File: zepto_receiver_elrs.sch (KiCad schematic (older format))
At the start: 43 parts, among them J1 u.fl, SW1 SW_Push, U1 STM32WLE5JBI6, U2 NCP160, U3 BGS12PL6E6327XTSA1, U4 0900FM15D0039, U5 ECS-TXO-25CSMV-320-AM-TR

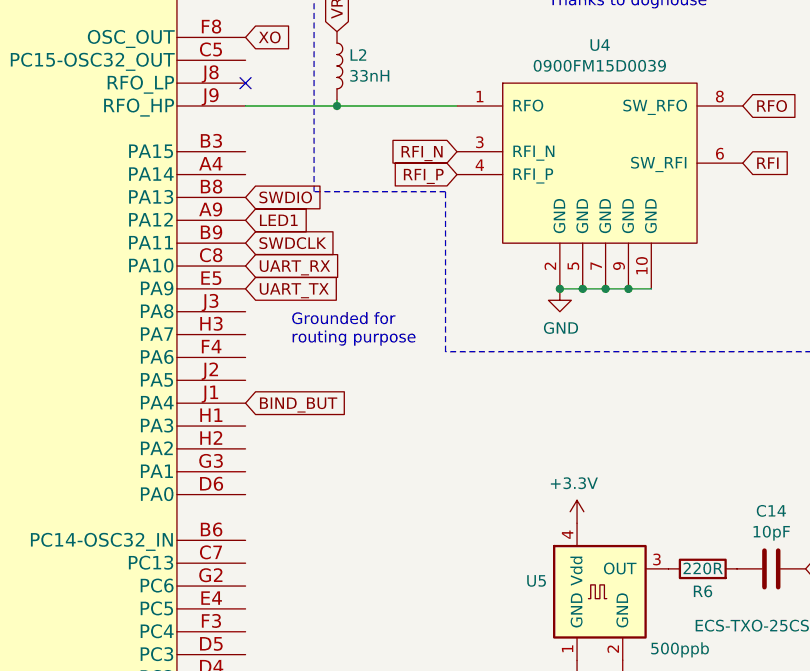
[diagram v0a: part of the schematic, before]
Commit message: update schematic and layout
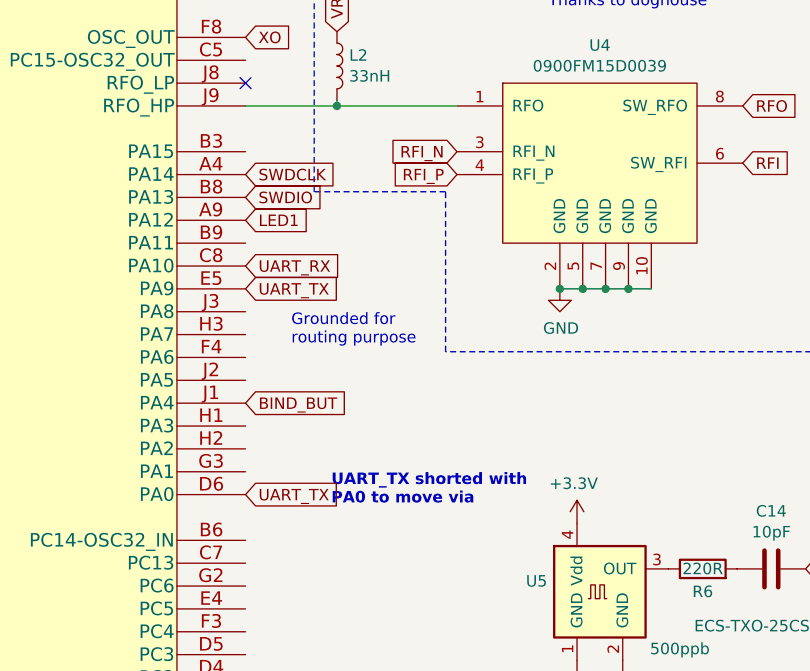
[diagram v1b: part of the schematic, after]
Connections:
- net SWDCLK: now also U1.A4 (PA14); no longer U1.B9 (PA11)
- net UART_TX: now also U1.D6 (PA0)
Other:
- note added: "UART_TX shorted with\nPA0 to move via"
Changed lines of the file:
@@
 EESchema Schematic File Version 4
-LIBS:zepto_receiver_elrs-cache
 EELAYER 30 0
 EELAYER END
@@
 Text GLabel 8000 1750 2    50   Input ~ 0
 SWDIO
-Text GLabel 8000 1950 2    50   Input ~ 0
+Text GLabel 8000 1650 2    50   Input ~ 0
 SWDCLK
+Text GLabel 8000 3050 2    50   Input ~ 0
+UART_TX
+Text Notes 8375 3100 0    50   ~ 10
+UART_TX shorted with\nPA0 to move via
 $EndSCHEMATC

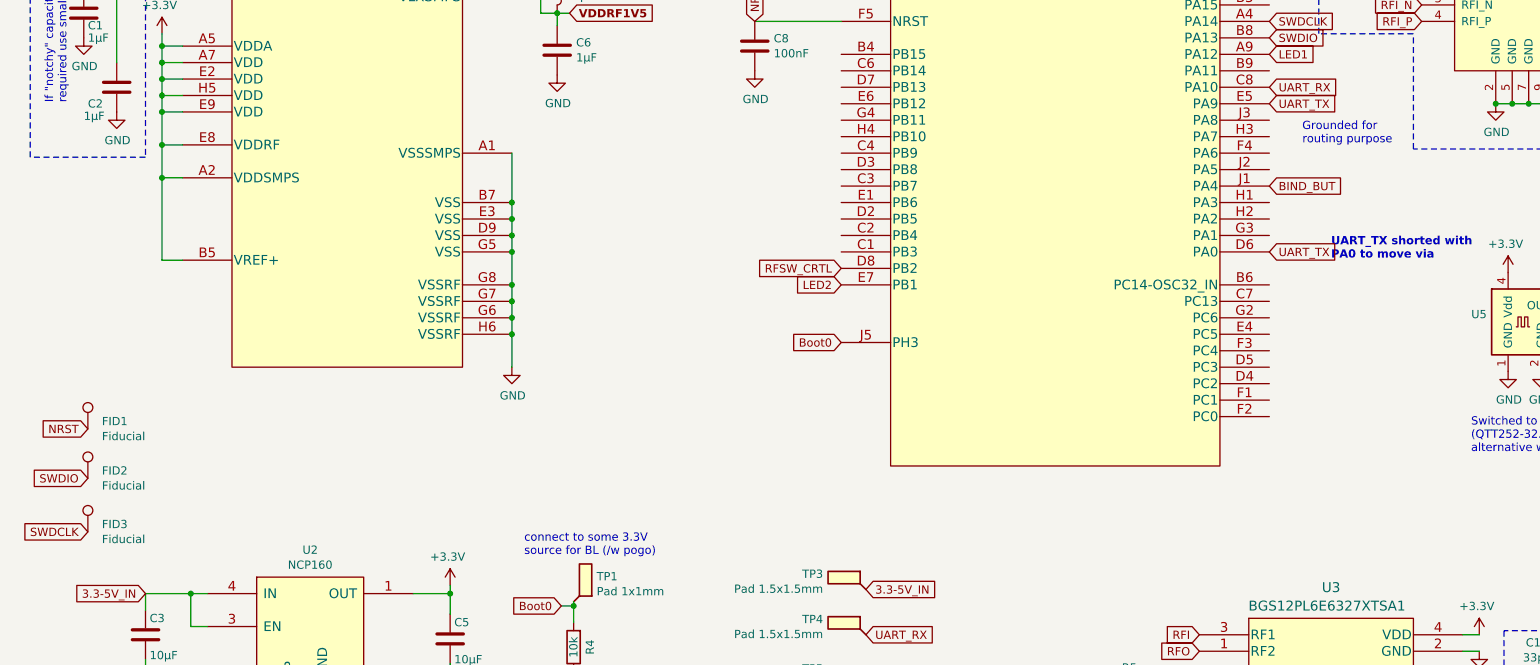
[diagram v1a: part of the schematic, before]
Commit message: moved a few components, checked pinout
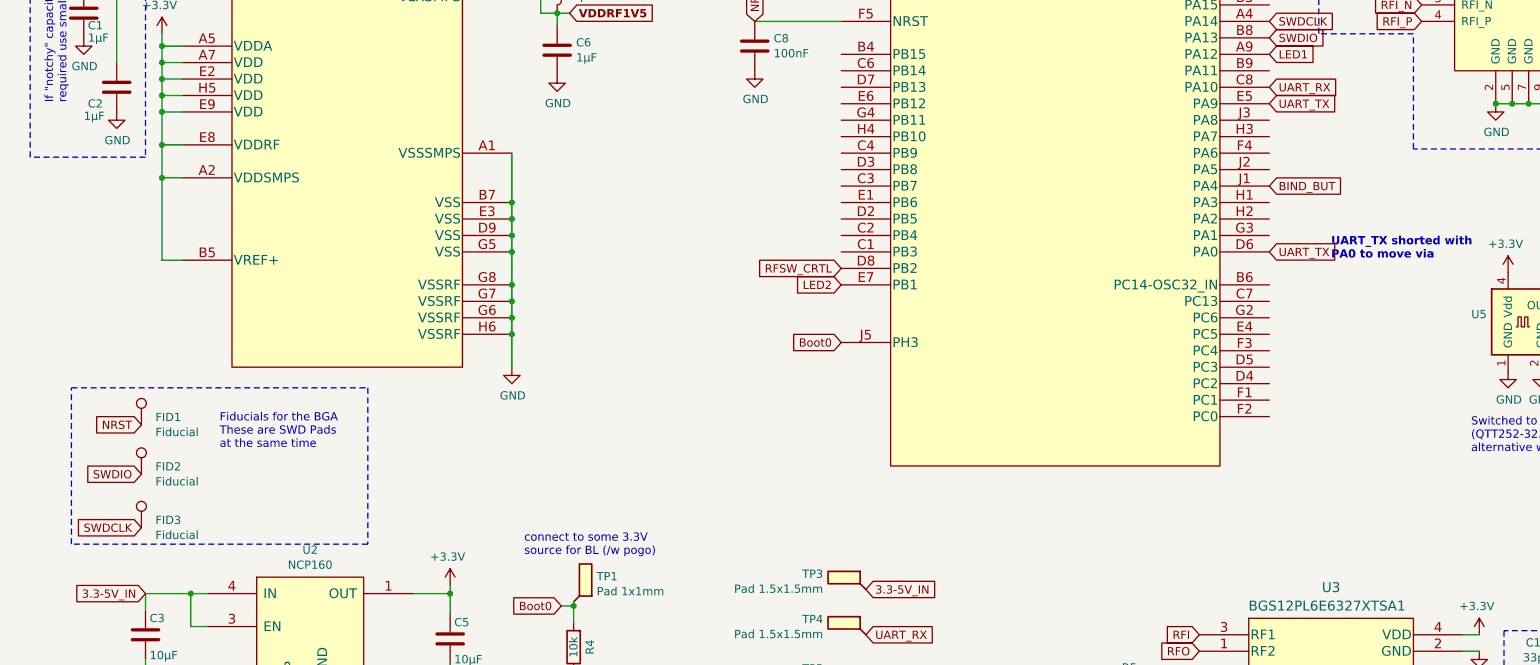
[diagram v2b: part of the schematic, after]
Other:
- note added: "Fiducials for the BGA\nThese are SWD Pads \nat the same time"
- note removed: "Grounded for \nrouting purpose"
- moved on the sheet: FID1, FID2, FID3
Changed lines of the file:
@@
 EESchema Schematic File Version 4
+LIBS:zepto_receiver_elrs-cache
 EELAYER 30 0
 EELAYER END
@@
 L Connector:TestPoint FID1
 U 1 1 6049244C
-P 825 4125
-F 0 "FID1" H 910 4171 50  0000 L CNN
-F 1 "Fiducial" H 910 4080 50  0000 L CNN
-F 2 "Fiducial:Fiducial_0.5mm_Dia_1mm_Outer" H 825 4125 50  0001 C CNN
-F 3 "~" H 825 4125 50  0001 C CNN
-F 4 "0" H 825 4125 50  0001 C CNN "BomCos@10k"
-	1    825  4125
+P 1150 4100
+F 0 "FID1" H 1235 4146 50  0000 L CNN
+F 1 "Fiducial" H 1235 4055 50  0000 L CNN
+F 2 "Fiducial:Fiducial_0.5mm_Dia_1mm_Outer" H 1150 4100 50  0001 C CNN
+F 3 "~" H 1150 4100 50  0001 C CNN
+F 4 "0" H 1150 4100 50  0001 C CNN "BomCos@10k"
+	1    1150 4100
 	1    0    0    -1
 $EndComp
@@
 L Connector:TestPoint FID2
 U 1 1 60493583
-P 825 4425
-F 0 "FID2" H 910 4471 50  0000 L CNN
-F 1 "Fiducial" H 910 4380 50  0000 L CNN
-F 2 "Fiducial:Fiducial_0.5mm_Dia_1mm_Outer" H 825 4425 50  0001 C CNN
-F 3 "~" H 825 4425 50  0001 C CNN
-F 4 "0" H 825 4425 50  0001 C CNN "BomCos@10k"
-	1    825  4425
-	1    0    0    -1
-$EndComp
-Text Notes 8200 2400 0    50   ~ 0
-Grounded for \nrouting purpose
+P 1150 4400
+F 0 "FID2" H 1235 4446 50  0000 L CNN
+F 1 "Fiducial" H 1235 4355 50  0000 L CNN
+F 2 "Fiducial:Fiducial_0.5mm_Dia_1mm_Outer" H 1150 4400 50  0001 C CNN
+F 3 "~" H 1150 4400 50  0001 C CNN
+F 4 "0" H 1150 4400 50  0001 C CNN "BomCos@10k"
+	1    1150 4400
+	1    0    0    -1
+$EndComp
 $Comp
 L sch_comp:0900FM15D0039 U4
@@
 L Connector:TestPoint FID3
 U 1 1 6056D526
-P 825 4750
-F 0 "FID3" H 910 4796 50  0000 L CNN
-F 1 "Fiducial" H 910 4705 50  0000 L CNN
-F 2 "Fiducial:Fiducial_0.5mm_Dia_1mm_Outer" H 825 4750 50  0001 C CNN
-F 3 "~" H 825 4750 50  0001 C CNN
-F 4 "0" H 825 4750 50  0001 C CNN "BomCos@10k"
-	1    825  4750
+P 1150 4725
+F 0 "FID3" H 1235 4771 50  0000 L CNN
+F 1 "Fiducial" H 1235 4680 50  0000 L CNN
+F 2 "Fiducial:Fiducial_0.5mm_Dia_1mm_Outer" H 1150 4725 50  0001 C CNN
+F 3 "~" H 1150 4725 50  0001 C CNN
+F 4 "0" H 1150 4725 50  0001 C CNN "BomCos@10k"
+	1    1150 4725
 	1    0    0    -1
 $EndComp
 Text GLabel 4875 1650 1    50   Input ~ 0
 NRST
-Text GLabel 825  4125 0    50   Input ~ 0
+Text GLabel 1150 4100 0    50   Input ~ 0
 NRST
-Text GLabel 825  4425 0    50   Input ~ 0
+Text GLabel 1150 4400 0    50   Input ~ 0
 SWDIO
-Text GLabel 825  4750 0    50   Input ~ 0
+Text GLabel 1150 4725 0    50   Input ~ 0
 SWDCLK
 Text GLabel 8000 1750 2    50   Input ~ 0
@@
 Text Notes 8375 3100 0    50   ~ 10
 UART_TX shorted with\nPA0 to move via
+Text Notes 1625 4250 0    50   ~ 0
+Fiducials for the BGA\nThese are SWD Pads \nat the same time
+Wire Notes Line
+	725  3875 2525 3875
+Wire Notes Line
+	2525 3875 2525 4825
+Wire Notes Line
+	2525 4825 725  4825
+Wire Notes Line
+	725  4825 725  3875
 $EndSCHEMATC

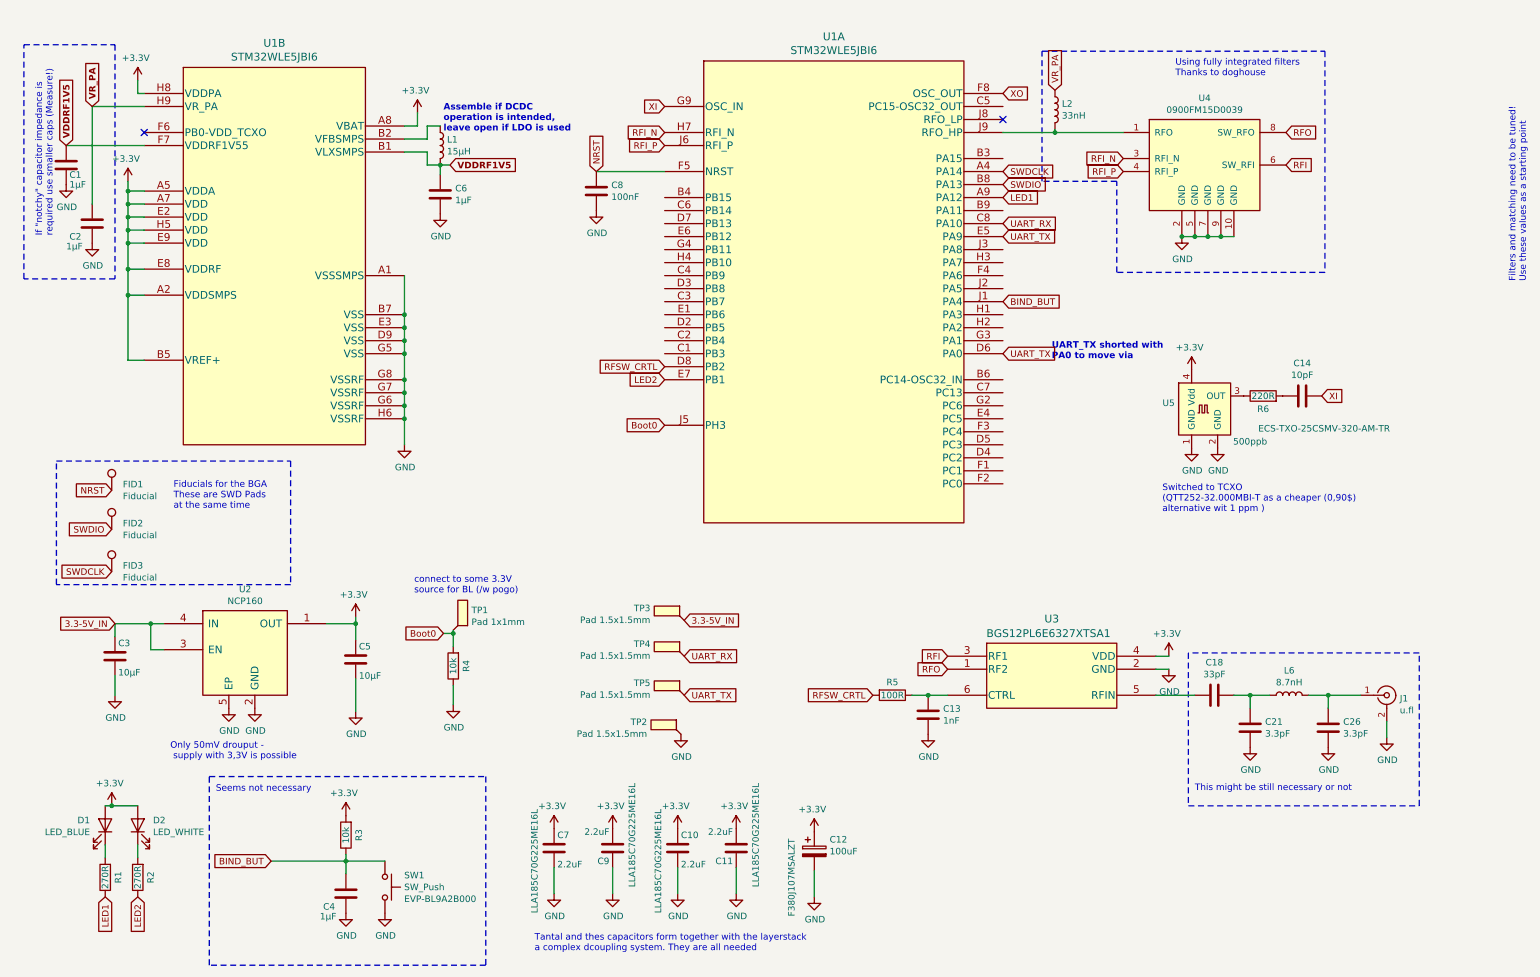
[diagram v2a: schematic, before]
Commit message: update sch, pdf and layout, add 3d views
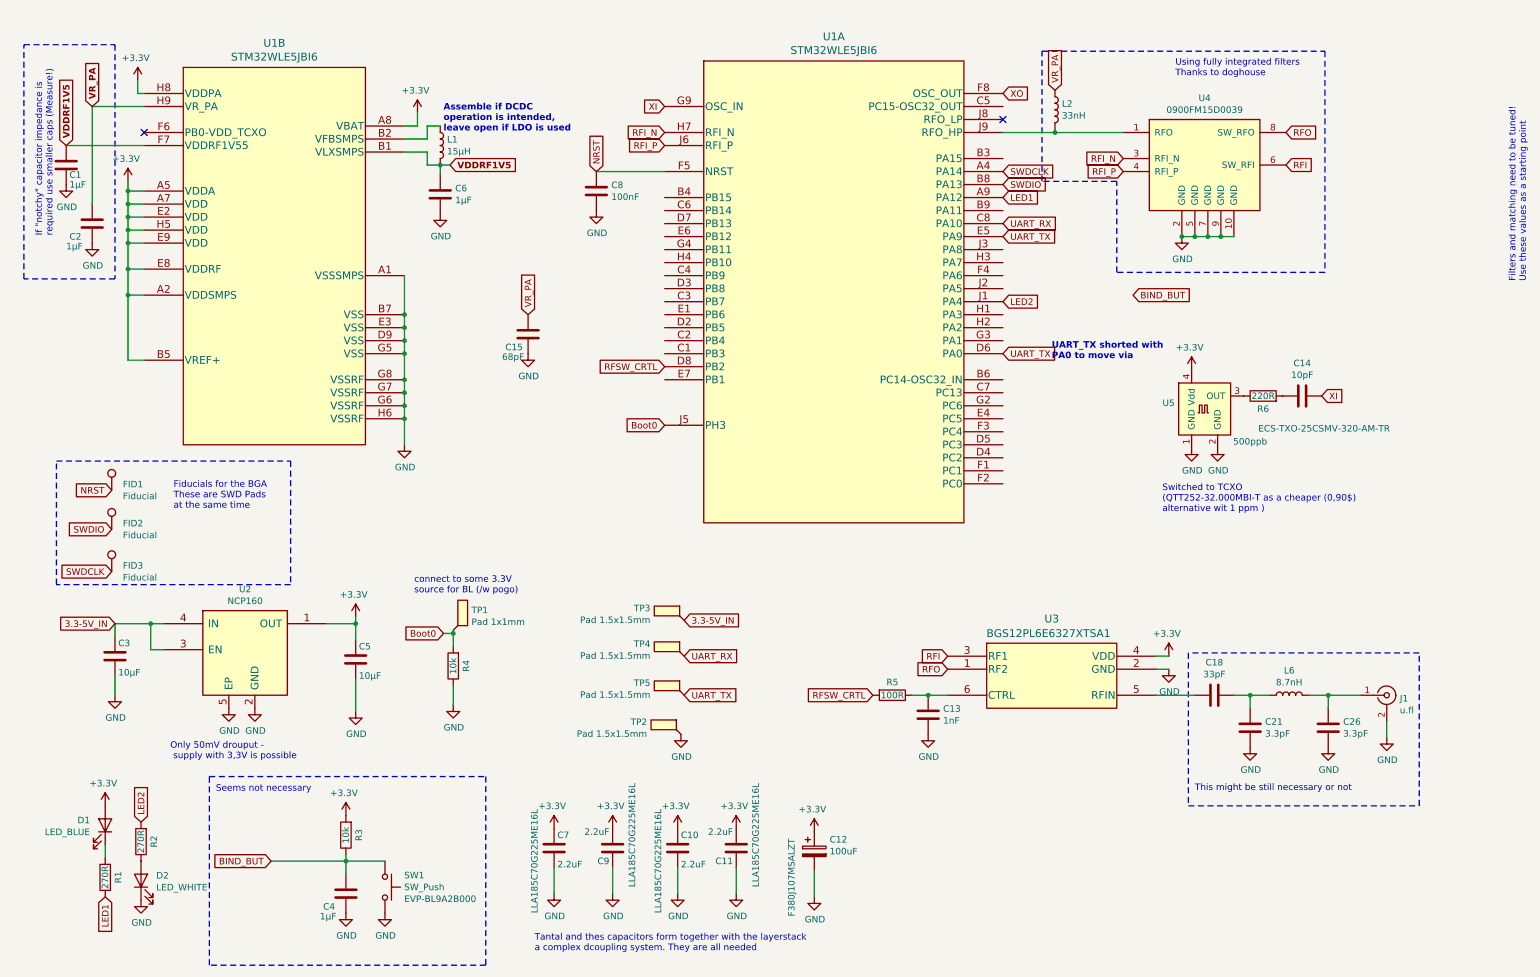
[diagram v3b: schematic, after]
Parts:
- added C15: 68pF, ftprnts:C_0201_0603Metric_dense, symbol Device:C
- TP2, TP3, TP4, TP5: footprint TestPoint:TestPoint_Pad_1.5x1.5mm -> ftprnts:TestPoint_Pad_1.5x2mm
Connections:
- net +3V3: no longer D2.2 (A)
- net BIND_BUT: no longer U1.J1 (PA4)
- net GND: now also D2.1 (K), C15.2
- net LED2: now also R2.2, U1.J1 (PA4); no longer R2.1, U1.E7 (PB1)
- net VR_PA: now also C15.1
- new net: D2.2 (A), R2.1
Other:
- moved on the sheet: D2, R2
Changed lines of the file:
@@
 EESchema Schematic File Version 4
-LIBS:zepto_receiver_elrs-cache
 EELAYER 30 0
 EELAYER END
@@
 Sheet 1 1
 Title ""
-Date "2021-03-10"
+Date "2021-03-13"
 Rev ""
 Comp ""
@@
 L power:+3.3V #PWR03
 U 1 1 6081FD31
-P 1150 6525
-F 0 "#PWR03" H 1150 6375 50  0001 C CNN
-F 1 "+3.3V" H 1165 6698 50  0000 C CNN
-F 2 "" H 1150 6525 50  0001 C CNN
-F 3 "" H 1150 6525 50  0001 C CNN
-	1    1150 6525
+P 1100 6525
+F 0 "#PWR03" H 1100 6375 50  0001 C CNN
+F 1 "+3.3V" H 1115 6698 50  0000 C CNN
+F 2 "" H 1100 6525 50  0001 C CNN
+F 3 "" H 1100 6525 50  0001 C CNN
+	1    1100 6525
 	-1   0    0    -1
 $EndComp
 Wire Wire Line
 	1100 6825 1100 6925
-Wire Wire Line
-	1350 6825 1350 6925
 Text GLabel 1100 7225 3    50   Input ~ 0
 LED1
-Text GLabel 1350 7225 3    50   Input ~ 0
-LED2
-Wire Wire Line
-	1100 6525 1150 6525
-Connection ~ 1150 6525
-Wire Wire Line
-	1150 6525 1350 6525
 Text GLabel 8000 1850 2    50   Input ~ 0
 LED1
-Text GLabel 5400 3250 0    50   Input ~ 0
+Text GLabel 8000 2650 2    50   Input ~ 0
 LED2
 $Comp
@@
 	1    0    0    -1
 $EndComp
-Text GLabel 8000 2650 2    50   Input ~ 0
+Text GLabel 9000 2600 2    50   Input ~ 0
 BIND_BUT
 $Comp
@@
 $EndComp
 $Comp
-L Device:LED D2
-U 1 1 6081EA93
-P 1350 6675
-F 0 "D2" V 1389 6558 50  0000 R CNN
-F 1 "LED_WHITE" V 1298 6558 50  0000 R CNN
-F 2 "LED_SMD:LED_0201_0603Metric" H 1350 6675 50  0001 C CNN
-F 3 "~" H 1350 6675 50  0001 C CNN
-F 4 "0,053" H 1350 6675 50  0001 C CNN "BomCos@10k"
-F 5 "LW QH8G-Q2OO-3K5L-1 " H 1350 6675 50  0001 C CNN "Type"
-	1    1350 6675
-	0    -1   -1   0
-$EndComp
-$Comp
 L Device:R R4
 U 1 1 6092D503
@@
 F 0 "TP2" H 5785 6069 50  0000 L CNN
 F 1 "Pad 1.5x1.5mm" H 5785 5978 50  0000 L CNN
-F 2 "TestPoint:TestPoint_Pad_1.5x1.5mm" H 5725 5975 50  0001 C CNN
+F 2 "ftprnts:TestPoint_Pad_1.5x2mm" H 5725 5975 50  0001 C CNN
 F 3 "~" H 5725 5975 50  0001 C CNN
 F 4 "0" H 5525 5975 50  0001 C CNN "BomCos@10k"
@@
 F 0 "TP5" H 5810 5769 50  0000 L CNN
 F 1 "Pad 1.5x1.5mm" H 5810 5678 50  0000 L CNN
-F 2 "TestPoint:TestPoint_Pad_1.5x1.5mm" H 5750 5675 50  0001 C CNN
+F 2 "ftprnts:TestPoint_Pad_1.5x2mm" H 5750 5675 50  0001 C CNN
 F 3 "~" H 5750 5675 50  0001 C CNN
 F 4 "0" H 5550 5675 50  0001 C CNN "BomCos@10k"
@@
 F 0 "TP4" H 5810 5469 50  0000 L CNN
 F 1 "Pad 1.5x1.5mm" H 5810 5378 50  0000 L CNN
-F 2 "TestPoint:TestPoint_Pad_1.5x1.5mm" H 5750 5375 50  0001 C CNN
+F 2 "ftprnts:TestPoint_Pad_1.5x2mm" H 5750 5375 50  0001 C CNN
 F 3 "~" H 5750 5375 50  0001 C CNN
 F 4 "0" H 5550 5375 50  0001 C CNN "BomCos@10k"
@@
 F 0 "TP3" H 5810 5194 50  0000 L CNN
 F 1 "Pad 1.5x1.5mm" H 5810 5103 50  0000 L CNN
-F 2 "TestPoint:TestPoint_Pad_1.5x1.5mm" H 5750 5100 50  0001 C CNN
+F 2 "ftprnts:TestPoint_Pad_1.5x2mm" H 5750 5100 50  0001 C CNN
 F 3 "~" H 5750 5100 50  0001 C CNN
 F 4 "0" H 5550 5100 50  0001 C CNN "BomCos@10k"
@@
 	1    5400 1150
 	1    0    0    -1
-$EndComp
-$Comp
-L Device:R R2
-U 1 1 60958642
-P 1350 7075
-F 0 "R2" V 1250 7075 50  0000 C CNN
-F 1 "270R" V 1350 7075 50  0000 C CNN
-F 2 "ftprnts:R_0201_0603Metric_dense" V 1280 7075 50  0001 C CNN
-F 3 "~" H 1350 7075 50  0001 C CNN
-F 4 "0,003" H 1350 7075 50  0001 C CNN "BomCos@10k"
-F 5 "RC0201FR-07270RL" H 1350 7075 50  0001 C CNN "Type"
-	1    1350 7075
-	-1   0    0    1
 $EndComp
 $Comp
@@
 Wire Notes Line
 	725  4825 725  3875
+Text GLabel 1375 6650 1    50   Input ~ 0
+LED2
+$Comp
+L power:GND #PWR0101
+U 1 1 60556B9C
+P 1375 7250
+F 0 "#PWR0101" H 1375 7000 50  0001 C CNN
+F 1 "GND" H 1380 7077 50  0000 C CNN
+F 2 "" H 1375 7250 50  0001 C CNN
+F 3 "" H 1375 7250 50  0001 C CNN
+	1    1375 7250
+	1    0    0    -1
+$EndComp
+$Comp
+L Device:R R2
+U 1 1 60958642
+P 1375 6800
+F 0 "R2" V 1275 6800 50  0000 C CNN
+F 1 "270R" V 1375 6800 50  0000 C CNN
+F 2 "ftprnts:R_0201_0603Metric_dense" V 1305 6800 50  0001 C CNN
+F 3 "~" H 1375 6800 50  0001 C CNN
+F 4 "0,003" H 1375 6800 50  0001 C CNN "BomCos@10k"
+F 5 "RC0201FR-07270RL" H 1375 6800 50  0001 C CNN "Type"
+	1    1375 6800
+	-1   0    0    1
+$EndComp
+$Comp
+L Device:LED D2
+U 1 1 6081EA93
+P 1375 7100
+F 0 "D2" V 1414 6983 50  0000 R CNN
+F 1 "LED_WHITE" V 1323 6983 50  0000 R CNN
+F 2 "LED_SMD:LED_0201_0603Metric" H 1375 7100 50  0001 C CNN
+F 3 "~" H 1375 7100 50  0001 C CNN
+F 4 "0,053" H 1375 7100 50  0001 C CNN "BomCos@10k"
+F 5 "LW QH8G-Q2OO-3K5L-1 " H 1375 7100 50  0001 C CNN "Type"
+	1    1375 7100
+	0    -1   -1   0
+$EndComp
+$Comp
+L Device:C C15
+U 1 1 6057CEF1
+P 4350 2900
+F 0 "C15" H 4175 2800 50  0000 L CNN
+F 1 "68pF" H 4150 2725 50  0000 L CNN
+F 2 "ftprnts:C_0201_0603Metric_dense" H 4388 2750 50  0001 C CNN
+F 3 "~" H 4350 2900 50  0001 C CNN
+F 4 "0,014" H 4350 2900 50  0001 C CNN "BomCos@10k"
+F 5 "GRM033C80J105ME05J" H 4350 2900 50  0001 C CNN "Type"
+	1    4350 2900
+	1    0    0    -1
+$EndComp
+Text GLabel 4350 2750 1    50   Input ~ 0
+VR_PA
+$Comp
+L power:GND #PWR0106
+U 1 1 6058AA62
+P 4350 3050
+F 0 "#PWR0106" H 4350 2800 50  0001 C CNN
+F 1 "GND" H 4355 2877 50  0000 C CNN
+F 2 "" H 4350 3050 50  0001 C CNN
+F 3 "" H 4350 3050 50  0001 C CNN
+	1    4350 3050
+	1    0    0    -1
+$EndComp
 $EndSCHEMATC
